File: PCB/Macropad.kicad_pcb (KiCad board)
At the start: 2 copper layers, 61.9 x 64.3 mm, 14 parts, among them SW1 SW_Push, SW2 SW_Push, SW3 SW_Push, SW4 SW_Push, SW5 SW_Push, SW6 SW_Push, SW7 RotaryEncoder_Switch, U1 XIAO-RP2040-DIP

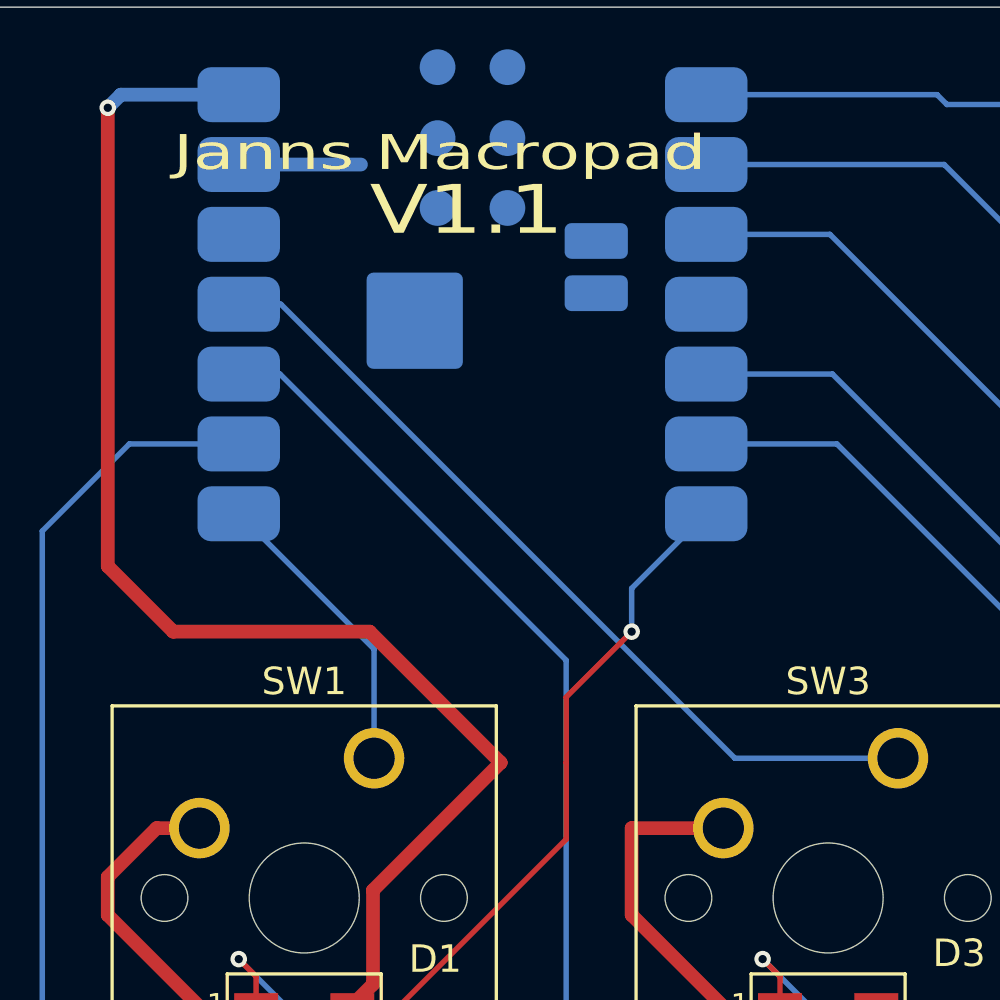
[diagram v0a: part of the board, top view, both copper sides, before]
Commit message: Fixed Faital Error with GND plate
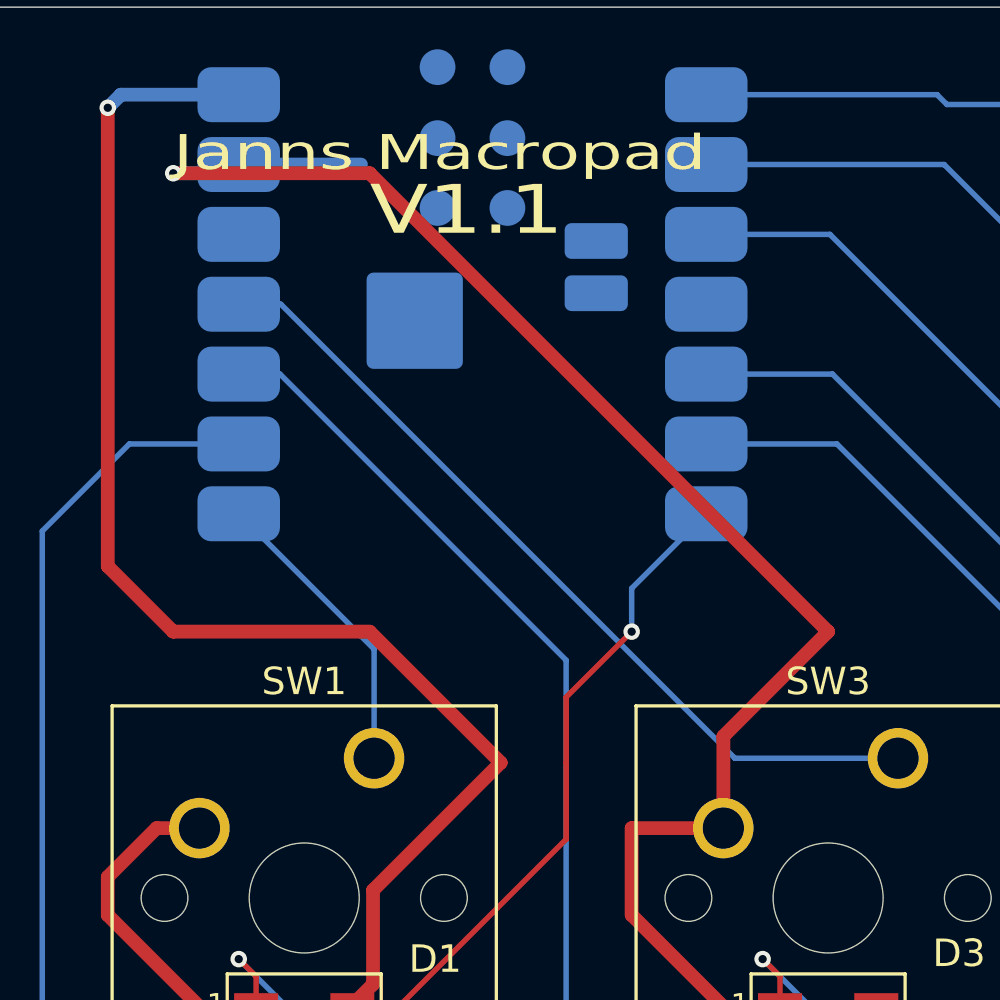
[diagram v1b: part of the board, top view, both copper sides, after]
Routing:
- net GND: track 86.1 -> 125.5 mm, vias 0 -> 1
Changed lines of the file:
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@@
 		)
+	)
+	(gr_line
+		(start 154.78125 61.9125)
+		(end 152.4 61.9125)
+		(stroke
+			(width 0.5)
+			(type solid)
+		)
+		(layer "B.Cu")
+		(net 4)
 	)
 	(gr_rect
@@
 	)
 	(segment
+		(start 172.4025 82.39125)
+		(end 172.4025 85.725)
+		(width 0.5)
+		(layer "F.Cu")
+		(net 4)
+	)
+	(segment
 		(start 174.4625 93.9025)
 		(end 174.0875 93.9025)
@@
 	)
 	(segment
+		(start 159.54375 61.9125)
+		(end 176.2125 78.58125)
+		(width 0.5)
+		(layer "F.Cu")
+		(net 4)
+	)
+	(segment
 		(start 150.01875 88.88575)
 		(end 155.0355 93.9025)
@@
 	)
 	(segment
+		(start 176.2125 78.58125)
+		(end 172.4025 82.39125)
+		(width 0.5)
+		(layer "F.Cu")
+		(net 4)
+	)
+	(segment
 		(start 193.1375 112.79375)
 		(end 188.11875 107.775)
@@
 		(net 4)
 	)
+	(segment
+		(start 152.4 61.9125)
+		(end 159.54375 61.9125)
+		(width 0.5)
+		(layer "F.Cu")
+		(net 4)
+	)
+	(via
+		(at 152.4 61.9125)
+		(size 0.6)
+		(drill 0.3)
+		(layers "F.Cu" "B.Cu")
+		(net 4)
+	)
